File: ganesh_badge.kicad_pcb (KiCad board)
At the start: 2 copper layers, 36 x 47.8 mm, 15 parts, among them J1 Conn_01x05_Male, J2 USB_B_Micro, SW1 SW_Push, U1 ATtiny9-TS

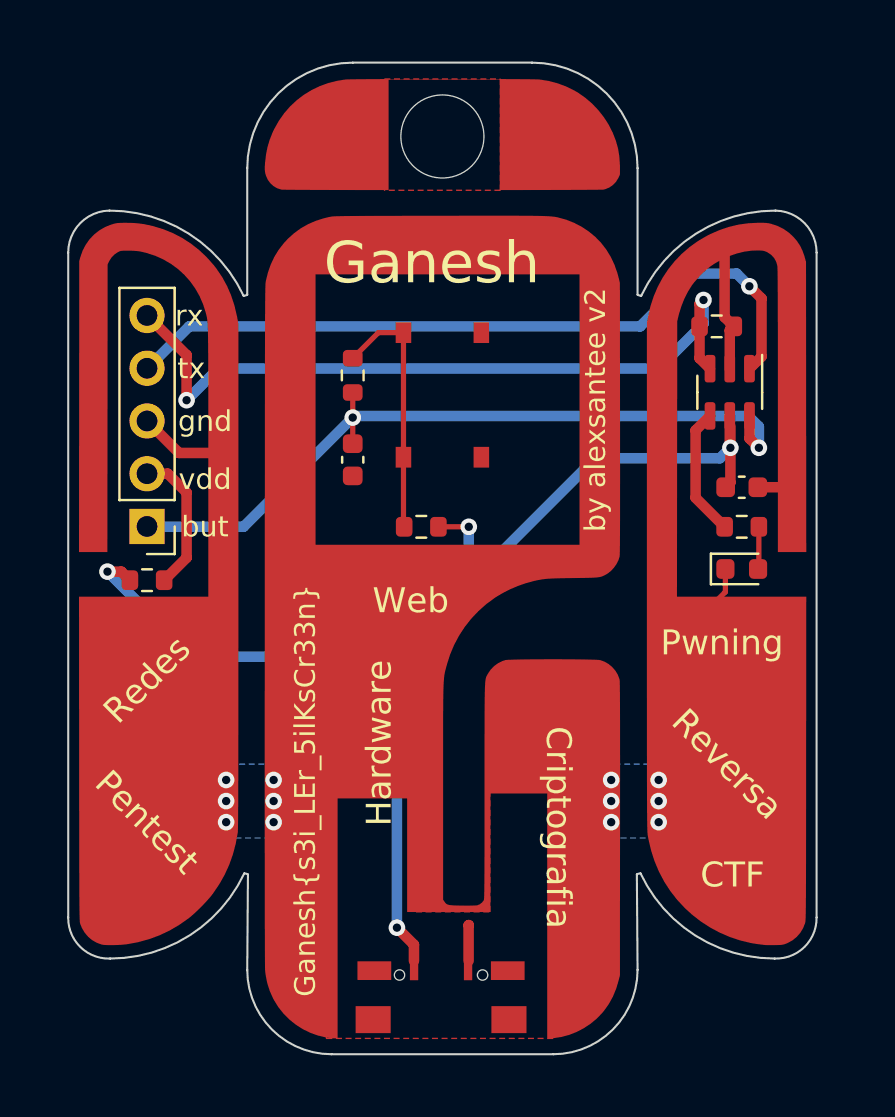
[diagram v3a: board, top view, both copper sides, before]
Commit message: added ground plane to back layer for aesthetics and better EMI
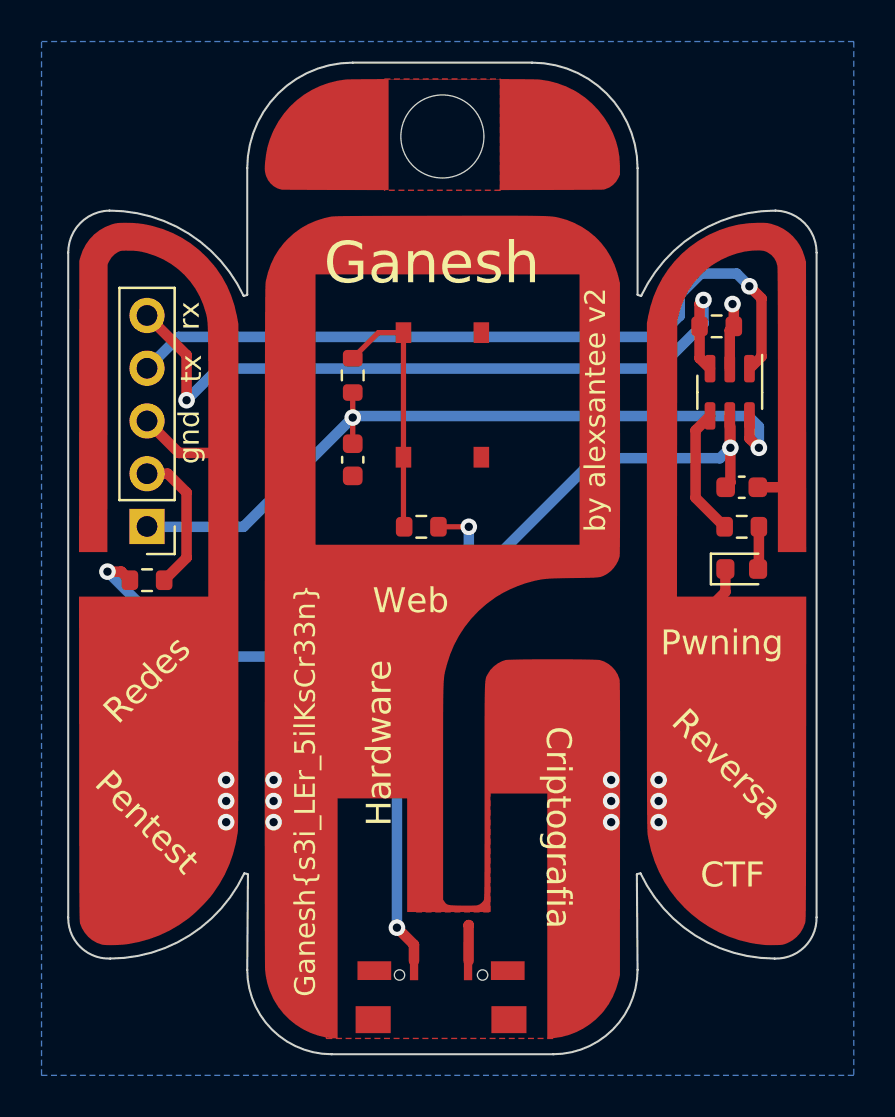
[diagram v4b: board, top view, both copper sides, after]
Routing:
- net GND: track 16.2 -> 12.4 mm, vias 12 -> 13
- net /tx: track 35.6 -> 36.2 mm
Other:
- board text removed: "but"
- board text removed: "vdd"
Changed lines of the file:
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@@
     (effects (font (size 1.2 1.2) (thickness 0.2)))
   )
-  (gr_text "but" (at 40.894 46.736) (layer "F.SilkS")
+  (gr_text "Hardware" (at 49.276 57.15 90) (layer "F.SilkS")
+    (effects (font (size 1.2 1.2) (thickness 0.2)))
+  )
+  (gr_text "Pwning" (at 65.786 52.324) (layer "F.SilkS")
+    (effects (font (size 1.2 1.2) (thickness 0.2)))
+  )
+  (gr_text "gnd" (at 40.132 42.418 90) (layer "F.SilkS")
     (effects (font (size 1 1) (thickness 0.16)))
   )
-  (gr_text "Hardware" (at 49.276 57.15 90) (layer "F.SilkS")
-    (effects (font (size 1.2 1.2) (thickness 0.2)))
-  )
-  (gr_text "Pwning" (at 65.786 52.324) (layer "F.SilkS")
-    (effects (font (size 1.2 1.2) (thickness 0.2)))
-  )
-  (gr_text "gnd" (at 40.894 41.656) (layer "F.SilkS")
-    (effects (font (size 1 1) (thickness 0.16)))
-  )
-  (gr_text "rx" (at 40.132 36.576) (layer "F.SilkS")
+  (gr_text "rx" (at 40.132 36.576 90) (layer "F.SilkS")
     (effects (font (size 1 1) (thickness 0.16)))
   )
@@
     (effects (font (size 2 2) (thickness 0.33)))
   )
-  (gr_text "vdd" (at 40.894 44.45) (layer "F.SilkS")
-    (effects (font (size 1 1) (thickness 0.16)))
-  )
   (gr_text "by alexsantee v2" (at 59.69 46.99 90) (layer "F.SilkS")
     (effects (font (size 1 1) (thickness 0.16)) (justify left))
   )
-  (gr_text "tx" (at 40.232 39.116) (layer "F.SilkS")
+  (gr_text "tx" (at 40.232 39.116 90) (layer "F.SilkS")
     (effects (font (size 1 1) (thickness 0.16)))
   )
@@
     (style (thickness 0.1) (arrow_length 1.27) (text_position_mode 0) (extension_height 0.58642) (extension_offset 0.5) keep_text_aligned)
   )
-  (segment (start 66.357 37.084) (end 65.913 36.64) (width 0.508) (layer "F.Cu") (net 1))
-  (segment (start 65.9515 49.8725) (end 65.024 50.8) (width 0.254) (layer "F.Cu") (net 1))
+  (segment (start 65.9515 49.8725) (end 65.532 50.292) (width 0.508) (layer "F.Cu") (net 1))
   (segment (start 67.514 44.831) (end 69.088 44.831) (width 0.508) (layer "F.Cu") (net 1))
   (segment (start 66.1615 39.1215) (end 66.1615 37.2795) (width 0.508) (layer "F.Cu") (net 1))
+  (segment (start 65.9515 48.768) (end 65.9515 49.8725) (width 0.508) (layer "F.Cu") (net 1))
   (segment (start 66.1615 37.2795) (end 66.357 37.084) (width 0.508) (layer "F.Cu") (net 1))
   (segment (start 53.594 65.913) (end 53.586298 65.920702) (width 0.508) (layer "F.Cu") (net 1))
-  (segment (start 65.913 36.64) (end 65.913 33.147) (width 0.508) (layer "F.Cu") (net 1))
+  (segment (start 66.357 37.084) (end 66.357 36.0725) (width 0.508) (layer "F.Cu") (net 1))
   (segment (start 53.586298 65.920702) (end 53.586298 67.637298) (width 0.508) (layer "F.Cu") (net 1))
+  (segment (start 66.357 36.0725) (end 66.294 36.0095) (width 0.508) (layer "F.Cu") (net 1))
   (segment (start 38.1 41.64) (end 39.64 43.18) (width 0.508) (layer "F.Cu") (net 1))
   (segment (start 39.64 43.18) (end 41.656 43.18) (width 0.508) (layer "F.Cu") (net 1))
-  (segment (start 65.9515 48.768) (end 65.9515 49.8725) (width 0.254) (layer "F.Cu") (net 1))
   (via (at 62.738 58.928) (size 0.8) (drill 0.4) (layers "F.Cu" "B.Cu") (free) (net 1))
   (via (at 60.452 60.96) (size 0.8) (drill 0.4) (layers "F.Cu" "B.Cu") (free) (net 1))
@@
   (via (at 41.91 59.944) (size 0.8) (drill 0.4) (layers "F.Cu" "B.Cu") (free) (net 1))
   (via (at 41.91 58.928) (size 0.8) (drill 0.4) (layers "F.Cu" "B.Cu") (free) (net 1))
+  (via (at 66.294 36.0095) (size 0.8) (drill 0.4) (layers "F.Cu" "B.Cu") (free) (net 1))
   (via (at 62.738 59.944) (size 0.8) (drill 0.4) (layers "F.Cu" "B.Cu") (free) (net 1))
   (via (at 60.452 58.928) (size 0.8) (drill 0.4) (layers "F.Cu" "B.Cu") (free) (net 1))
   (via (at 44.196 60.96) (size 0.8) (drill 0.4) (layers "F.Cu" "B.Cu") (free) (net 1))
-  (segment (start 67.564 48.7305) (end 67.5265 48.768) (width 0.254) (layer "F.Cu") (net 2))
-  (segment (start 67.564 46.736) (end 67.564 48.7305) (width 0.254) (layer "F.Cu") (net 2))
+  (segment (start 67.564 48.7305) (end 67.5265 48.768) (width 0.508) (layer "F.Cu") (net 2))
+  (segment (start 67.564 46.736) (end 67.564 48.7305) (width 0.508) (layer "F.Cu") (net 2))
   (segment (start 64.707 37.084) (end 64.707 36.004) (width 0.508) (layer "F.Cu") (net 3))
   (segment (start 64.707 36.004) (end 64.897 35.814) (width 0.508) (layer "F.Cu") (net 3))
@@
   (segment (start 67.691 35.7378) (end 67.1068 35.1536) (width 0.508) (layer "F.Cu") (net 4))
   (via (at 67.1068 35.1536) (size 0.8) (drill 0.4) (layers "F.Cu" "B.Cu") (free) (net 4))
-  (segment (start 61.849 37.084) (end 40.132 37.084) (width 0.508) (layer "B.Cu") (net 4))
-  (segment (start 40.132 37.084) (end 38.116 39.1) (width 0.508) (layer "B.Cu") (net 4))
-  (segment (start 67.1068 35.1536) (end 66.4972 34.544) (width 0.508) (layer "B.Cu") (net 4))
-  (segment (start 64.389 34.544) (end 61.849 37.084) (width 0.508) (layer "B.Cu") (net 4))
-  (segment (start 38.116 39.1) (end 38.1 39.1) (width 0.508) (layer "B.Cu") (net 4))
-  (segment (start 66.4972 34.544) (end 64.389 34.544) (width 0.508) (layer "B.Cu") (net 4))
+  (segment (start 66.4972 34.544) (end 67.1068 35.1536) (width 0.508) (layer "B.Cu") (net 4))
+  (segment (start 63.754 36.576) (end 63.754 35.56) (width 0.508) (layer "B.Cu") (net 4))
+  (segment (start 39.624 37.592) (end 62.738 37.592) (width 0.508) (layer "B.Cu") (net 4))
+  (segment (start 38.116 39.1) (end 39.624 37.592) (width 0.508) (layer "B.Cu") (net 4))
+  (segment (start 63.754 35.56) (end 64.77 34.544) (width 0.508) (layer "B.Cu") (net 4))
+  (segment (start 38.1 39.1) (end 38.116 39.1) (width 0.508) (layer "B.Cu") (net 4))
+  (segment (start 62.738 37.592) (end 63.754 36.576) (width 0.508) (layer "B.Cu") (net 4))
+  (segment (start 64.77 34.544) (end 66.4972 34.544) (width 0.508) (layer "B.Cu") (net 4))
   (segment (start 52.133 46.736) (end 53.594 46.736) (width 0.254) (layer "F.Cu") (net 5))
   (segment (start 50.955 66.860502) (end 50.955 67.645) (width 0.508) (layer "F.Cu") (net 5))
@@
   )
   (zone (net 1) (net_name "GND") (layer "B.Cu") (hatch edge 0.508)
-    (connect_pads yes (clearance 0.508))
-    (min_thickness 0.254) (filled_areas_thickness no)
-    (fill yes (thermal_gap 0.508) (thermal_bridge_width 0.508) (island_removal_mode 1) (island_area_min 0))
-    (polygon
-      (pts
-        (xy 44.958 61.722)
-        (xy 41.148 61.722)
-        (xy 41.148 58.166)
-        (xy 44.958 58.166)
-      )
-    )
-  )
-  (zone (net 1) (net_name "GND") (layer "B.Cu") (hatch edge 0.508)
-    (connect_pads yes (clearance 0.508))
-    (min_thickness 0.254) (filled_areas_thickness no)
-    (fill yes (thermal_gap 0.508) (thermal_bridge_width 0.508) (island_removal_mode 1) (island_area_min 0))
-    (polygon
-      (pts
-        (xy 63.5 61.722)
-        (xy 59.69 61.722)
-        (xy 59.69 58.166)
-        (xy 63.5 58.166)
-      )
-    )
+    (connect_pads (clearance 0.508))
+    (min_thickness 0.254) (filled_areas_thickness no)
+    (fill yes (thermal_gap 0.508) (thermal_bridge_width 0.508))
+    (polygon
+      (pts
+        (xy 72.136 73.152)
+        (xy 33.02 73.152)
+        (xy 33.02 23.368)
+        (xy 72.136 23.368)
+      )
+    )
